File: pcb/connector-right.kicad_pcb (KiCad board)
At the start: 2 copper layers, 7.8 x 48.8 mm, 4 parts, among them J11 Conn_01x12_Socket, J9 Conn_01x12_Socket

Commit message: second draft
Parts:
- H3, H4: footprint zzkeeb:Hole_M2-TH -> zzkeeb:Hole_M2-solder-nut-2.5

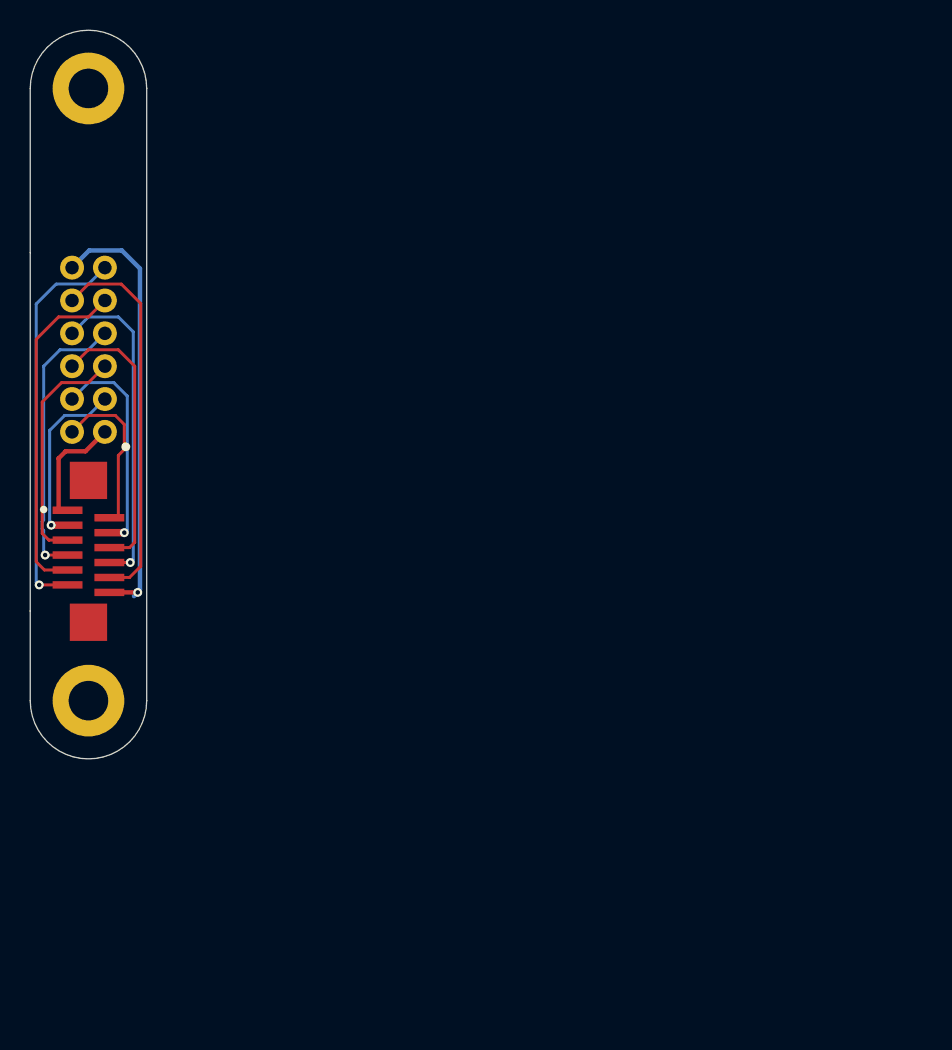
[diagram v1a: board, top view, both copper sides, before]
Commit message: add 3d components
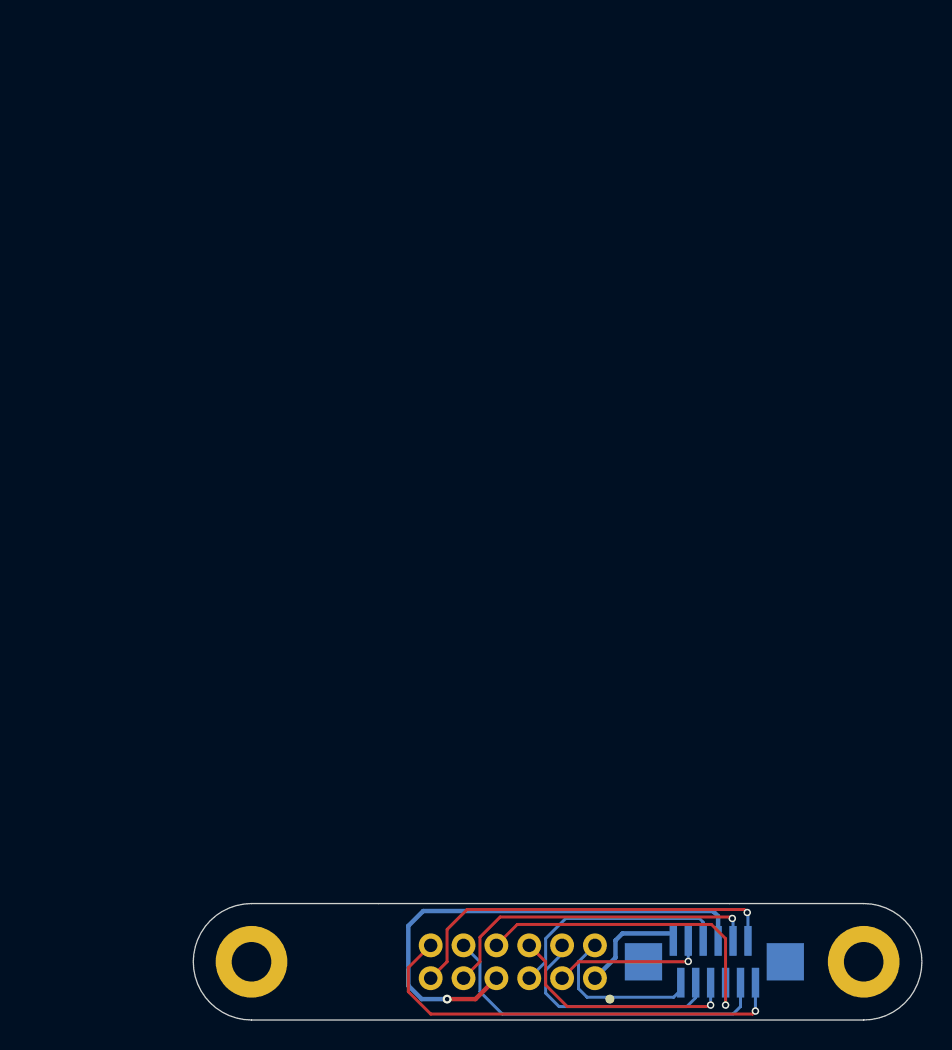
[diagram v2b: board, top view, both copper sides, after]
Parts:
- H3, H4: moved to B.Cu
- J11: moved to F.Cu
- J9: value Conn_01x12_Socket -> C262499; moved to B.Cu
- moved H3 59.5 mm to (84.9, 101.9), turned to -90 degrees
- moved H4 54.8 mm to (125.9, 101.9), turned to -90 degrees
- moved J9 50.1 mm to (115.9, 101.9), turned to 180 degrees
- moved J11 49.9 mm to (102.4, 101.9), turned to 90 degrees
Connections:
- J11 pad 1: (no net) -> BAT-conn2
- J11 pad 10: (no net) -> row1-conn2
- J11 pad 11: (no net) -> row0-conn2
- J11 pad 12: GND -> free-conn2
- J11 pad 2: (no net) -> col4-conn2
- J11 pad 3: (no net) -> col3-conn2
- J11 pad 4: (no net) -> col2-conn2
- J11 pad 5: (no net) -> col1-conn2
- J11 pad 6: (no net) -> col0-conn2
- J11 pad 7: (no net) -> GND
- J11 pad 8: (no net) -> row3-conn2
- J11 pad 9: (no net) -> row2-conn2
- J9 pad 1: (no net) -> free-conn2
- J9 pad 10: (no net) -> col3-conn2
- J9 pad 11: (no net) -> col4-conn2
- J9 pad 12: GND -> BAT-conn2
- J9 pad 2: (no net) -> row0-conn2
- J9 pad 3: (no net) -> row1-conn2
- J9 pad 4: (no net) -> row2-conn2
- J9 pad 5: (no net) -> row3-conn2
- J9 pad 6: (no net) -> GND
- J9 pad 7: (no net) -> col0-conn2
- J9 pad 8: (no net) -> col1-conn2
- J9 pad 9: (no net) -> col2-conn2
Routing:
- net (no net): track 191.3 -> 0.00 mm, vias 5 -> 0
- net free-conn2: track 0.00 -> 29.1 mm, vias 0 -> 1
- net row0-conn2: track 0.00 -> 25.9 mm, vias 0 -> 1
- net row1-conn2: track 0.00 -> 22.9 mm
- net row2-conn2: track 0.00 -> 21.8 mm, vias 0 -> 1
- net row3-conn2: track 0.00 -> 21.8 mm, vias 0 -> 1
- net col0-conn2: track 0.00 -> 15.8 mm, vias 0 -> 1
- net col1-conn2: track 0.00 -> 15.1 mm
- net col2-conn2: track 0.00 -> 14.8 mm
- net col3-conn2: track 0.00 -> 10.8 mm, vias 0 -> 1
- net col4-conn2: track 0.00 -> 10.6 mm
- net BAT-conn2: track 0.00 -> 7.17 mm
- net GND: track 29.0 -> 33.8 mm
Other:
- board size 7.8 x 48.8 mm -> 48.8 x 7.8 mm
